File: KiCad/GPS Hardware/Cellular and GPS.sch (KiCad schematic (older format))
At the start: 30 parts, among them J3 Conn_Coaxial, Q1 BC847, Q2 BC847, Q3 BSS84, U10 ublox_SAM-M8Q, U7 74AVC2T245GU-Q100X, U8 SARA-U201

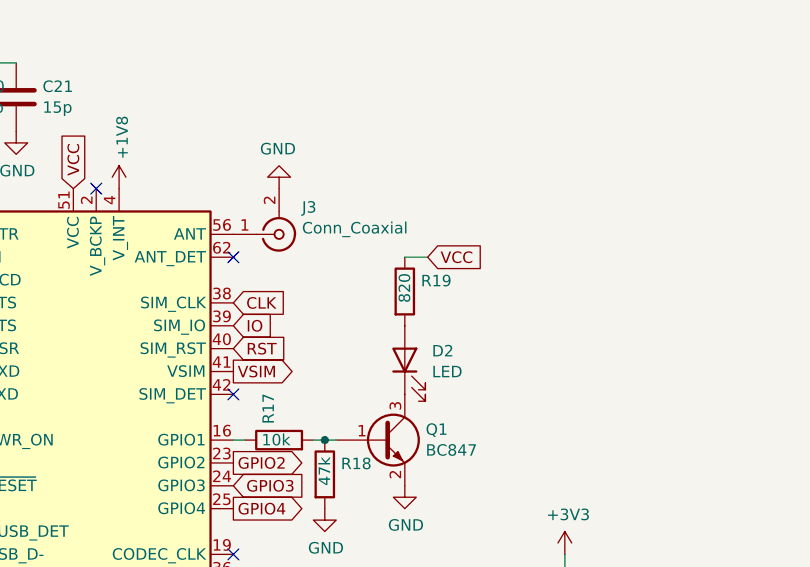
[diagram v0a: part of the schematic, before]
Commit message: Changed resistor values for LEDs
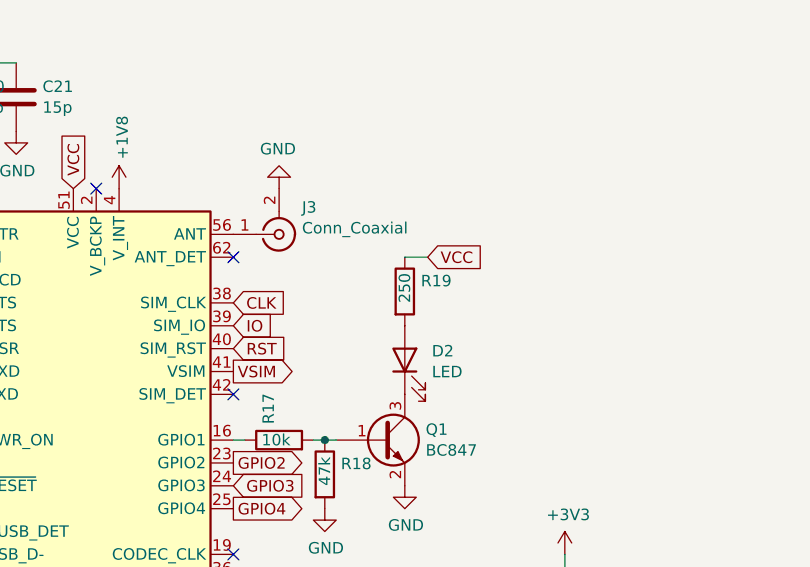
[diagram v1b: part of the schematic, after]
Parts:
- R19: value 820 -> 250
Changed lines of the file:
@@
 AR Path="/613BCFF5/615E2B7B" Ref="R19"  Part="1"
 F 0 "R19" H 4520 2246 50  0000 L CNN
-F 1 "820" V 4450 2150 50  0000 L CNN
+F 1 "250" V 4450 2150 50  0000 L CNN
 F 2 "Resistor_SMD:R_0603_1608Metric_Pad0.98x0.95mm_HandSolder" V 4380 2200 50  0001 C CNN
 F 3 "~" H 4450 2200 50  0001 C CNN
@@
 F 1 "SIM8065-6-1-14-01-A_REVA1" H 9280 4105 50  0000 L CNN
 F 2 "GCT_SIM8065-6-1-14-01-A_REVA1" H 9050 4150 50  0001 L BNN
-F 3 "" H 9050 4150 50  0001 L BNN
+F 3 "https://www.mouser.co.uk/datasheet/2/837/SIM8065_spec-2327472.pdf" H 9050 4150 50  0001 L BNN
 F 4 "1.37 mm" H 9050 4150 50  0001 L BNN "MAXIMUM_PACKAGE_HEIGHT"
 F 5 "A1" H 9050 4150 50  0001 L BNN "PARTREV"
